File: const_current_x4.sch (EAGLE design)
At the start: 21 parts

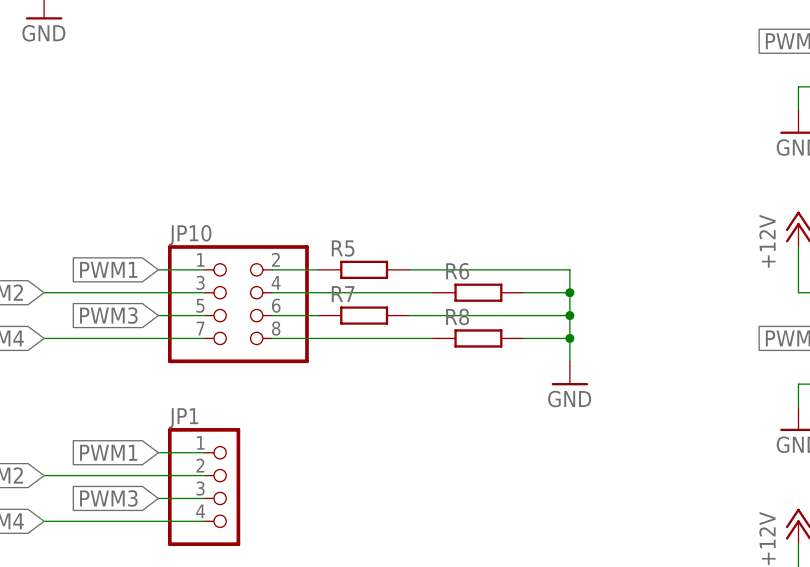
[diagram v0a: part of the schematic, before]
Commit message: Fixed bug in routing of Out- for the constant current modules
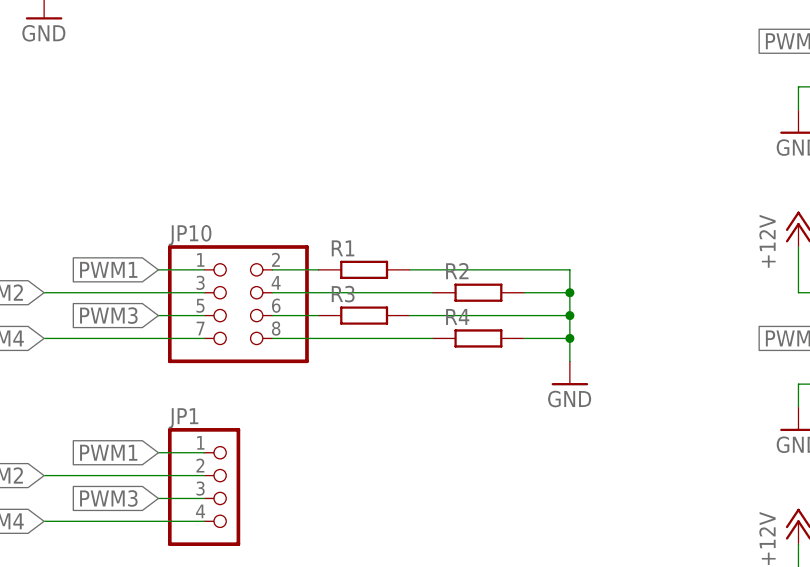
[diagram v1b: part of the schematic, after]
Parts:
- renumbered R5 to R1, R6 to R2, R7 to R3, R8 to R4
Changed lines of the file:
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@@
 <part name="GND2" library="supply1" deviceset="GND" device=""/>
 <part name="JP10" library="pinhead" deviceset="PINHD-2X4" device=""/>
-<part name="R5" library="resistor" deviceset="R-EU_" device="0207/10"/>
-<part name="R6" library="resistor" deviceset="R-EU_" device="0207/10"/>
-<part name="R7" library="resistor" deviceset="R-EU_" device="0207/10"/>
-<part name="R8" library="resistor" deviceset="R-EU_" device="0207/10"/>
+<part name="R1" library="resistor" deviceset="R-EU_" device="0207/10"/>
+<part name="R2" library="resistor" deviceset="R-EU_" device="0207/10"/>
+<part name="R3" library="resistor" deviceset="R-EU_" device="0207/10"/>
+<part name="R4" library="resistor" deviceset="R-EU_" device="0207/10"/>
 <part name="GND12" library="supply1" deviceset="GND" device=""/>
 <part name="JP1" library="pinhead" deviceset="PINHD-1X4" device=""/>
@@
 <instance part="GND2" gate="1" x="66.04" y="152.4"/>
 <instance part="JP10" gate="A" x="111.76" y="119.38"/>
-<instance part="R5" gate="G$1" x="127" y="124.46"/>
-<instance part="R6" gate="G$1" x="139.7" y="121.92"/>
-<instance part="R7" gate="G$1" x="127" y="119.38"/>
-<instance part="R8" gate="G$1" x="139.7" y="116.84"/>
+<instance part="R1" gate="G$1" x="127" y="124.46"/>
+<instance part="R2" gate="G$1" x="139.7" y="121.92"/>
+<instance part="R3" gate="G$1" x="127" y="119.38"/>
+<instance part="R4" gate="G$1" x="139.7" y="116.84"/>
 <instance part="GND12" gate="1" x="149.86" y="111.76"/>
 <instance part="JP1" gate="A" x="111.76" y="99.06"/>
@@
 </segment>
 <segment>
-<pinref part="R5" gate="G$1" pin="2"/>
+<pinref part="R1" gate="G$1" pin="2"/>
 <wire x1="132.08" y1="124.46" x2="149.86" y2="124.46" width="0.1524" layer="91"/>
 <wire x1="149.86" y1="124.46" x2="149.86" y2="121.92" width="0.1524" layer="91"/>
 <pinref part="GND12" gate="1" pin="GND"/>
-<pinref part="R6" gate="G$1" pin="2"/>
+<pinref part="R2" gate="G$1" pin="2"/>
 <wire x1="149.86" y1="121.92" x2="149.86" y2="119.38" width="0.1524" layer="91"/>
 <wire x1="149.86" y1="119.38" x2="149.86" y2="116.84" width="0.1524" layer="91"/>
@@
 <wire x1="144.78" y1="121.92" x2="149.86" y2="121.92" width="0.1524" layer="91"/>
 <junction x="149.86" y="121.92"/>
-<pinref part="R7" gate="G$1" pin="2"/>
+<pinref part="R3" gate="G$1" pin="2"/>
 <wire x1="132.08" y1="119.38" x2="149.86" y2="119.38" width="0.1524" layer="91"/>
 <junction x="149.86" y="119.38"/>
-<pinref part="R8" gate="G$1" pin="2"/>
+<pinref part="R4" gate="G$1" pin="2"/>
 <wire x1="144.78" y1="116.84" x2="149.86" y2="116.84" width="0.1524" layer="91"/>
 <junction x="149.86" y="116.84"/>
@@
 <segment>
 <pinref part="JP10" gate="A" pin="2"/>
-<pinref part="R5" gate="G$1" pin="1"/>
+<pinref part="R1" gate="G$1" pin="1"/>
 <wire x1="121.92" y1="124.46" x2="116.84" y2="124.46" width="0.1524" layer="91"/>
 </segment>
@@
 <segment>
 <pinref part="JP10" gate="A" pin="4"/>
-<pinref part="R6" gate="G$1" pin="1"/>
+<pinref part="R2" gate="G$1" pin="1"/>
 <wire x1="134.62" y1="121.92" x2="116.84" y2="121.92" width="0.1524" layer="91"/>
 </segment>
@@
 <segment>
 <pinref part="JP10" gate="A" pin="6"/>
-<pinref part="R7" gate="G$1" pin="1"/>
+<pinref part="R3" gate="G$1" pin="1"/>
 <wire x1="121.92" y1="119.38" x2="116.84" y2="119.38" width="0.1524" layer="91"/>
 </segment>
@@
 <segment>
 <pinref part="JP10" gate="A" pin="8"/>
-<pinref part="R8" gate="G$1" pin="1"/>
+<pinref part="R4" gate="G$1" pin="1"/>
 <wire x1="134.62" y1="116.84" x2="116.84" y2="116.84" width="0.1524" layer="91"/>
 </segment>
